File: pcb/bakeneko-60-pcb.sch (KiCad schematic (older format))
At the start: 18 parts, among them J1 JST SH 4-pin, J2 AVR-ISP-6, SW1 Reset, U1 USBLC6-2SC6, U2 ATmega32U4-AU, Y1 16MHz

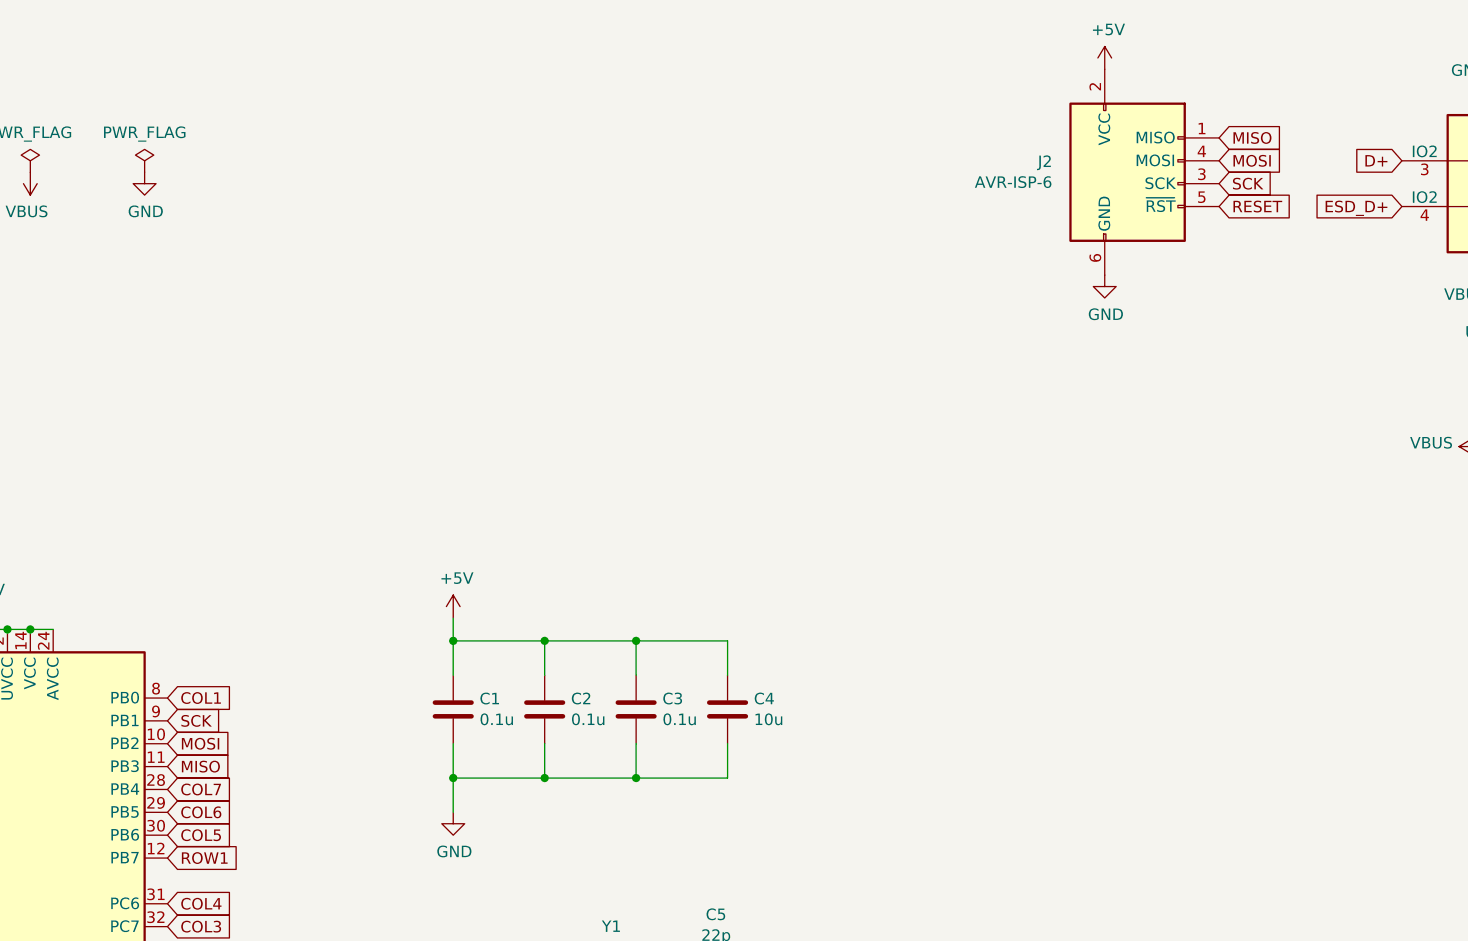
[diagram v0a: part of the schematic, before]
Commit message: Remove ISP
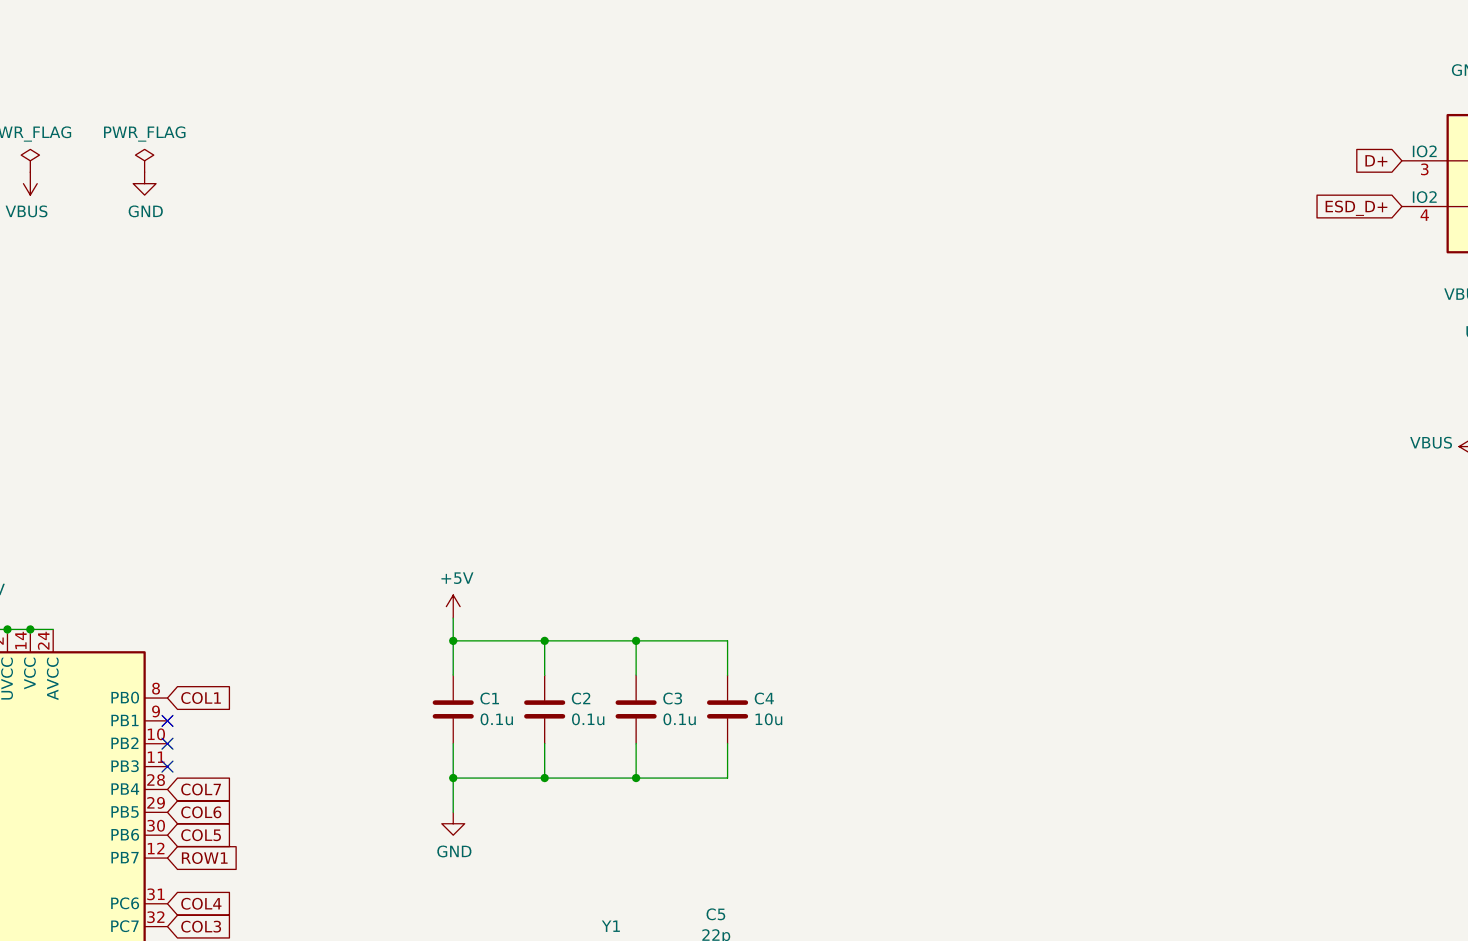
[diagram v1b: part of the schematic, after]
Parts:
- removed J2: AVR-ISP-6, random-keyboard-parts:Reset_Pretty, symbol Connector:AVR-ISP-6
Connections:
- net MISO: no longer names the net of U2.11 (PB3)
- net MOSI: no longer names the net of U2.10 (PB2)
- net SCK: no longer names the net of U2.9 (PB1)
- no-connect marks 3 -> 6
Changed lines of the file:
@@
 Wire Wire Line
 	5050 5400 5500 5400
-$Comp
-L Connector:AVR-ISP-6 J2
-U 1 1 5F4C9CCE
-P 7150 1650
-F 0 "J2" H 6821 1746 50  0000 R CNN
-F 1 "AVR-ISP-6" H 6821 1655 50  0000 R CNN
-F 2 "random-keyboard-parts:Reset_Pretty" V 6900 1700 50  0001 C CNN
-F 3 " ~" H 5875 1100 50  0001 C CNN
-	1    7150 1650
-	1    0    0    -1
-$EndComp
-$Comp
-L power:GND #PWR08
-U 1 1 5F4D2BF6
-P 7050 2050
-F 0 "#PWR08" H 7050 1800 50  0001 C CNN
-F 1 "GND" H 7055 1877 50  0000 C CNN
-F 2 "" H 7050 2050 50  0001 C CNN
-F 3 "" H 7050 2050 50  0001 C CNN
-	1    7050 2050
-	1    0    0    -1
-$EndComp
-Text GLabel 7550 1450 2    50   Input ~ 0
-MISO
-Text GLabel 7550 1550 2    50   Input ~ 0
-MOSI
-Text GLabel 7550 1650 2    50   Input ~ 0
-SCK
-Text GLabel 7550 1750 2    50   Input ~ 0
-RESET
-Text GLabel 2950 4200 2    50   Input ~ 0
-MISO
-Text GLabel 2950 4000 2    50   Input ~ 0
-SCK
-Text GLabel 2950 4100 2    50   Input ~ 0
-MOSI
 Text GLabel 2950 5200 2    50   Input ~ 0
 COL14
@@
 $EndComp
 $Comp
-L power:+5V #PWR01
-U 1 1 5F3D1A13
-P 7050 1150
-F 0 "#PWR01" H 7050 1000 50  0001 C CNN
-F 1 "+5V" H 7065 1323 50  0000 C CNN
-F 2 "" H 7050 1150 50  0001 C CNN
-F 3 "" H 7050 1150 50  0001 C CNN
-	1    7050 1150
-	1    0    0    -1
-$EndComp
-$Comp
 L power:+5V #PWR021
 U 1 1 5F3DDD9D
@@
 ROW3
 NoConn ~ 2950 5100
+NoConn ~ 2950 4200
+NoConn ~ 2950 4100
+NoConn ~ 2950 4000
 $EndSCHEMATC
